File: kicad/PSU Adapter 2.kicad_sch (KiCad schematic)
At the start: 17 parts, among them J1 AC Connector, J2 ATX From PSU, J3 Power to Logic Board, J4 Fan, J5 Power to PSU, J6 Conn_01x05_Pin, K1 AC Passthrough Relay, U1 TLP521-1

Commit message: Add files via upload
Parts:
- removed J2: ATX From PSU, Connector_Molex:Molex_Mini-Fit_Jr_5566-20A_2x10_P4.20mm_Vertical, symbol Connector:ATX-20
- added J7: ATX-24, Connector_Molex:Molex_Mini-Fit_Jr_5566-24A_2x12_P4.20mm_Vertical, symbol Connector:ATX-24
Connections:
- net +12V: now also J7.10 (+12V), J7.11 (+12V)
- net +5V: now also J7.21 (+5V), J7.22 (+5V), J7.23 (+5V), J7.4 (+5V), J7.6 (+5V)
- net +5VSB: now also J7.9 (+5VSB)
- net -12V: now also J7.14 (-12V)
- net GND: now also J7.15 (GND), J7.17 (GND), J7.18 (GND), J7.19 (GND), J7.24 (GND), J7.3 (GND), J7.5 (GND), J7.7 (GND)
- net PS_ON: now also J7.16 (PS_ON#)
- net PWR_OK: now also J7.8 (PWR_OK)
- new net: J7.1 (+3.3V), J7.12 (+3.3V), J7.13 (+3.3V), J7.2 (+3.3V)
- no-connect marks 7 -> 6
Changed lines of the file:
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@@
+	)
+	(no_connect
+		(at 59.69 147.32)
+	)
+	(no_connect
+		(at 59.69 132.08)
+	)
+	(no_connect
+		(at 59.69 156.21)
+	)
+	(no_connect
+		(at 48.26 99.06)
 	)
 	(no_connect
@@
 	)
 	(no_connect
-		(at 59.69 147.32)
-	)
-	(no_connect
-		(at 59.69 132.08)
-	)
-	(no_connect
-		(at 59.69 156.21)
-	)
-	(no_connect
-		(at 48.26 99.06)
-	)
-	(no_connect
 		(at 59.69 139.7)
-	)
-	(no_connect
-		(at 162.56 106.68)
 	)
 	(wire
@@
 	)
 	(symbol
-		(lib_id "Connector:ATX-20")
+		(lib_id "Connector:ATX-24")
 		(at 149.86 99.06 0)
 		(unit 1)
@@
 		(dnp no)
 		(fields_autoplaced yes)
-		(property "Reference" "J2"
+		(property "Reference" "J7"
 			(at 149.86 81.28 0)
 			(effects
@@
 			)
 		)
-		(property "Value" "ATX From PSU"
+		(property "Value" "ATX-24"
 			(at 149.86 83.82 0)
 			(effects
@@
 			)
 		)
-		(property "Footprint" "Connector_Molex:Molex_Mini-Fit_Jr_5566-20A_2x10_P4.20mm_Vertical"
+		(property "Footprint" "Connector_Molex:Molex_Mini-Fit_Jr_5566-24A_2x12_P4.20mm_Vertical"
 			(at 149.86 101.6 0)
 			(effects
@@
 			)
 		)
-		(property "Datasheet" "https://web.aub.edu.lb/pub/docs/atx_201.pdf#page=20"
-			(at 177.8 113.03 0)
-			(effects
-				(font
-					(size 1.27 1.27)
-				)
-				(hide yes)
-			)
-		)
-		(property "Description" "ATX Power supply 20pins"
+		(property "Datasheet" "https://www.intel.com/content/dam/www/public/us/en/documents/guides/power-supply-design-guide-june.pdf#page=33"
+			(at 210.82 113.03 0)
+			(effects
+				(font
+					(size 1.27 1.27)
+				)
+				(hide yes)
+			)
+		)
+		(property "Description" "ATX Power supply 24pins"
 			(at 149.86 99.06 0)
 			(effects
@@
 			)
 		)
+		(pin "22"
+		)
+		(pin "4"
+		)
+		(pin "16"
+		)
+		(pin "6"
+		)
+		(pin "5"
+		)
+		(pin "24"
+		)
+		(pin "21"
+		)
+		(pin "3"
+		)
+		(pin "23"
+		)
+		(pin "17"
+		)
+		(pin "19"
+		)
+		(pin "9"
+		)
+		(pin "12"
+		)
+		(pin "18"
+		)
+		(pin "7"
+		)
+		(pin "1"
+		)
+		(pin "13"
+		)
+		(pin "14"
+		)
+		(pin "8"
+		)
+		(pin "10"
+		)
+		(pin "11"
+		)
 		(pin "2"
 		)
-		(pin "5"
+		(pin "15"
 		)
 		(pin "20"
-		)
-		(pin "8"
-		)
-		(pin "6"
-		)
-		(pin "7"
-		)
-		(pin "9"
-		)
-		(pin "4"
-		)
-		(pin "14"
-		)
-		(pin "15"
-		)
-		(pin "12"
-		)
-		(pin "18"
-		)
-		(pin "19"
-		)
-		(pin "17"
-		)
-		(pin "3"
-		)
-		(pin "16"
-		)
-		(pin "11"
-		)
-		(pin "10"
-		)
-		(pin "1"
-		)
-		(pin "13"
 		)
 		(instances
 			(project ""
 				(path "/aa6810f0-306b-47aa-aed9-06c517ff2e59"
-					(reference "J2")
+					(reference "J7")
 					(unit 1)
 				)

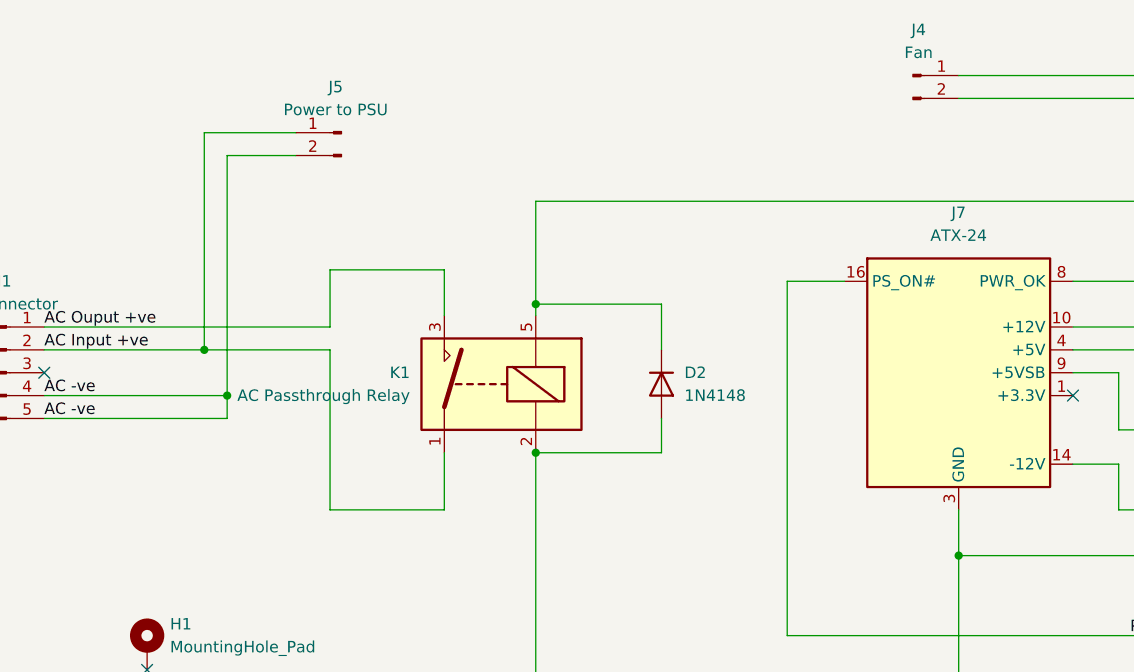
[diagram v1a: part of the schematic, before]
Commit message: Add files via upload
Updated to rev 0.3 including footprint for Chinese ATX connector which has 4.2mm pitch between rows (Molex spec is 5.5mm)
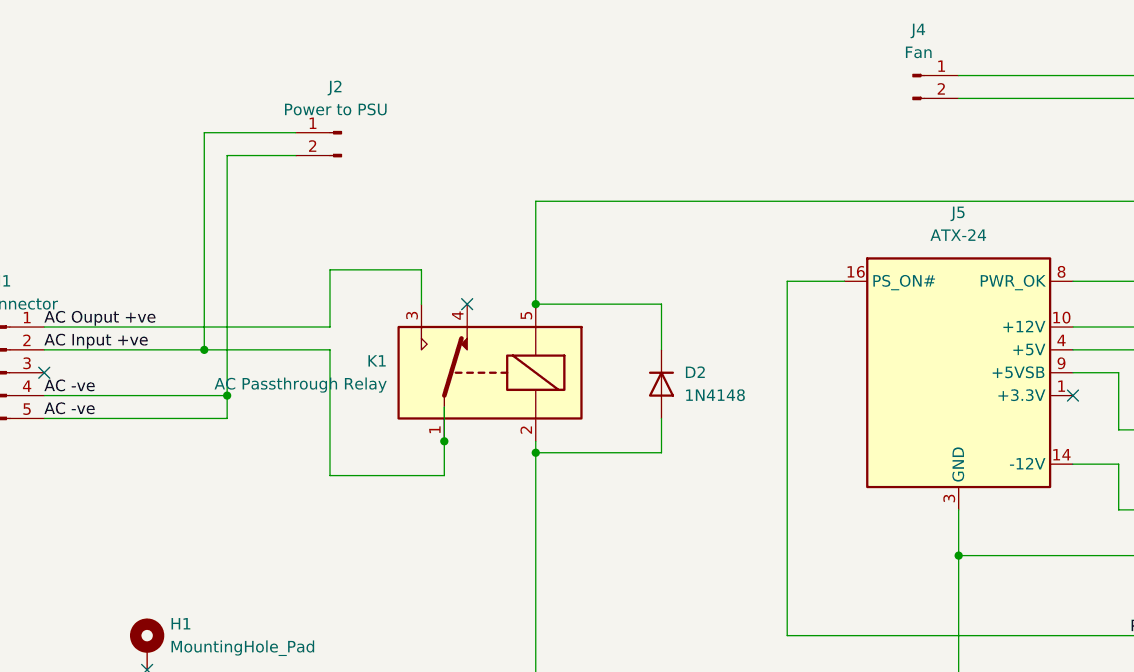
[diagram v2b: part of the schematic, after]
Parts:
- removed K1: AC Passthrough Relay, Relay_THT:Relay_SPST_SANYOU_SRD_Series_Form_A, symbol Relay:SANYOU_SRD_Form_A
- added K1: AC Passthrough Relay, Relay_THT:Relay_SPDT_SANYOU_SRD_Series_Form_C, symbol Relay:SANYOU_SRD_Form_C
- J4: footprint Connector_JST:JST_PH_B2B-PH-K_1x02_P2.00mm_Vertical -> Connector_JST:JST_XA_B02B-XASK-1-A_1x02_P2.50mm_Vertical
- renumbered J5 to J2, J7 to J5
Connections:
- net +12V: now also K1.5
- net AC Input +ve: now also K1.1
- net AC Ouput +ve: now also K1.3
- net GND: now also K1.2
- no-connect marks 6 -> 7
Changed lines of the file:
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@@
+	)
+	(junction
+		(at 177.8 123.19)
+		(diameter 0)
+		(color 0 0 0 0)
+	)
+	(junction
+		(at 233.68 101.6)
+		(diameter 0)
+		(color 0 0 0 0)
+	)
+	(junction
+		(at 149.86 134.62)
+		(diameter 0)
+		(color 0 0 0 0)
+	)
+	(junction
+		(at 177.8 73.66)
+		(diameter 0)
+		(color 0 0 0 0)
+	)
+	(junction
+		(at 92.71 106.68)
+		(diameter 0)
+		(color 0 0 0 0)
+	)
+	(junction
+		(at 173.99 80.01)
+		(diameter 0)
+		(color 0 0 0 0)
+	)
+	(junction
+		(at 200.66 130.81)
+		(diameter 0)
+		(color 0 0 0 0)
 	)
 	(junction
@@
 	)
 	(junction
-		(at 177.8 123.19)
-		(diameter 0)
-		(color 0 0 0 0)
-	)
-	(junction
-		(at 233.68 101.6)
-		(diameter 0)
-		(color 0 0 0 0)
-	)
-	(junction
-		(at 149.86 134.62)
-		(diameter 0)
-		(color 0 0 0 0)
-	)
-	(junction
-		(at 177.8 73.66)
-		(diameter 0)
-		(color 0 0 0 0)
-	)
-	(junction
-		(at 173.99 80.01)
-		(diameter 0)
-		(color 0 0 0 0)
-	)
-	(junction
-		(at 200.66 130.81)
-		(diameter 0)
-		(color 0 0 0 0)
-	)
-	(junction
 		(at 102.87 107.95)
 		(diameter 0)
@@
 	)
 	(no_connect
+		(at 95.25 91.44)
+	)
+	(no_connect
 		(at 162.56 101.6)
 	)
@@
 	(wire
 		(pts
-			(xy 80.01 96.52) (xy 80.01 114.3)
+			(xy 80.01 96.52) (xy 80.01 110.49)
 		)
 		(stroke
@@
 	(wire
 		(pts
-			(xy 92.71 87.63) (xy 92.71 92.71)
+			(xy 90.17 87.63) (xy 90.17 91.44)
 		)
 		(stroke
@@
 	(wire
 		(pts
-			(xy 102.87 91.44) (xy 102.87 92.71)
-		)
-		(stroke
-			(width 0)
-			(type default)
-		)
-	)
-	(wire
-		(pts
-			(xy 80.01 87.63) (xy 92.71 87.63)
+			(xy 102.87 106.68) (xy 102.87 107.95)
+		)
+		(stroke
+			(width 0)
+			(type default)
+		)
+	)
+	(wire
+		(pts
+			(xy 80.01 87.63) (xy 90.17 87.63)
 		)
 		(stroke
@@
 	(wire
 		(pts
-			(xy 92.71 114.3) (xy 80.01 114.3)
+			(xy 92.71 110.49) (xy 80.01 110.49)
 		)
 		(stroke
@@
 	(wire
 		(pts
-			(xy 92.71 107.95) (xy 92.71 114.3)
+			(xy 92.71 102.87) (xy 92.71 106.68)
 		)
 		(stroke
@@
 		(pts
 			(xy 116.84 104.14) (xy 116.84 107.95)
+		)
+		(stroke
+			(width 0)
+			(type default)
+		)
+	)
+	(wire
+		(pts
+			(xy 92.71 106.68) (xy 92.71 110.49)
 		)
 		(stroke
@@
 		(on_board yes)
 		(dnp no)
-		(property "Reference" "J5"
+		(property "Reference" "J2"
 			(at 80.645 67.31 0)
 			(effects
@@
 			(project ""
 				(path "/aa6810f0-306b-47aa-aed9-06c517ff2e59"
-					(reference "J5")
+					(reference "J2")
 					(unit 1)
 				)
@@
 				(path "/aa6810f0-306b-47aa-aed9-06c517ff2e59"
 					(reference "D2")
+					(unit 1)
+				)
+			)
+		)
+	)
+	(symbol
+		(lib_id "Relay:SANYOU_SRD_Form_C")
+		(at 97.79 99.06 0)
+		(mirror y)
+		(unit 1)
+		(exclude_from_sim no)
+		(in_bom yes)
+		(on_board yes)
+		(dnp no)
+		(property "Reference" "K1"
+			(at 86.36 97.7899 0)
+			(effects
+				(font
+					(size 1.27 1.27)
+				)
+				(justify left)
+			)
+		)
+		(property "Value" "AC Passthrough Relay"
+			(at 86.36 100.3299 0)
+			(effects
+				(font
+					(size 1.27 1.27)
+				)
+				(justify left)
+			)
+		)
+		(property "Footprint" "Relay_THT:Relay_SPDT_SANYOU_SRD_Series_Form_C"
+			(at 86.36 100.33 0)
+			(effects
+				(font
+					(size 1.27 1.27)
+				)
+				(justify left)
+				(hide yes)
+			)
+		)
+		(property "Datasheet" "http://www.sanyourelay.ca/public/products/pdf/SRD.pdf"
+			(at 97.79 99.06 0)
+			(effects
+				(font
+					(size 1.27 1.27)
+				)
+				(hide yes)
+			)
+		)
+		(property "Description" "Sanyo SRD relay, Single Pole Miniature Power Relay,"
+			(at 97.79 99.06 0)
+			(effects
+				(font
+					(size 1.27 1.27)
+				)
+				(hide yes)
+			)
+		)
+		(pin "3"
+		)
+		(pin "5"
+		)
+		(pin "2"
+		)
+		(pin "1"
+		)
+		(pin "4"
+		)
+		(instances
+			(project ""
+				(path "/aa6810f0-306b-47aa-aed9-06c517ff2e59"
+					(reference "K1")
 					(unit 1)
 				)
@@
 	)
 	(symbol
-		(lib_id "Relay:SANYOU_SRD_Form_A")
-		(at 97.79 100.33 0)
-		(mirror y)
-		(unit 1)
-		(exclude_from_sim no)
-		(in_bom yes)
-		(on_board yes)
-		(dnp no)
-		(property "Reference" "K1"
-			(at 88.9 99.0599 0)
-			(effects
-				(font
-					(size 1.27 1.27)
-				)
-				(justify left)
-			)
-		)
-		(property "Value" "AC Passthrough Relay"
-			(at 88.9 101.5999 0)
-			(effects
-				(font
-					(size 1.27 1.27)
-				)
-				(justify left)
-			)
-		)
-		(property "Footprint" "Relay_THT:Relay_SPST_SANYOU_SRD_Series_Form_A"
-			(at 88.9 101.6 0)
-			(effects
-				(font
-					(size 1.27 1.27)
-				)
-				(justify left)
-				(hide yes)
-			)
-		)
-		(property "Datasheet" "http://www.sanyourelay.ca/public/products/pdf/SRD.pdf"
-			(at 97.79 100.33 0)
-			(effects
-				(font
-					(size 1.27 1.27)
-				)
-				(hide yes)
-			)
-		)
-		(property "Description" "Sanyo SRD relay, Single Pole Miniature Power Relay, Closing Contact"
-			(at 97.79 100.33 0)
-			(effects
-				(font
-					(size 1.27 1.27)
-				)
-				(hide yes)
-			)
-		)
-		(pin "3"
-		)
-		(pin "2"
-		)
-		(pin "1"
-		)
-		(pin "5"
-		)
-		(instances
-			(project ""
-				(path "/aa6810f0-306b-47aa-aed9-06c517ff2e59"
-					(reference "K1")
-					(unit 1)
-				)
-			)
-		)
-	)
-	(symbol
 		(lib_id "Connector:ATX-24")
 		(at 149.86 99.06 0)
@@
 		(dnp no)
 		(fields_autoplaced yes)
-		(property "Reference" "J7"
+		(property "Reference" "J5"
 			(at 149.86 81.28 0)
 			(effects
@@
 			(project ""
 				(path "/aa6810f0-306b-47aa-aed9-06c517ff2e59"
-					(reference "J7")
+					(reference "J5")
 					(unit 1)
 				)
@@
 			)
 		)
-		(property "Footprint" "Connector_JST:JST_PH_B2B-PH-K_1x02_P2.00mm_Vertical"
+		(property "Footprint" "Connector_JST:JST_XA_B02B-XASK-1-A_1x02_P2.50mm_Vertical"
 			(at 144.78 66.04 0)
 			(effects

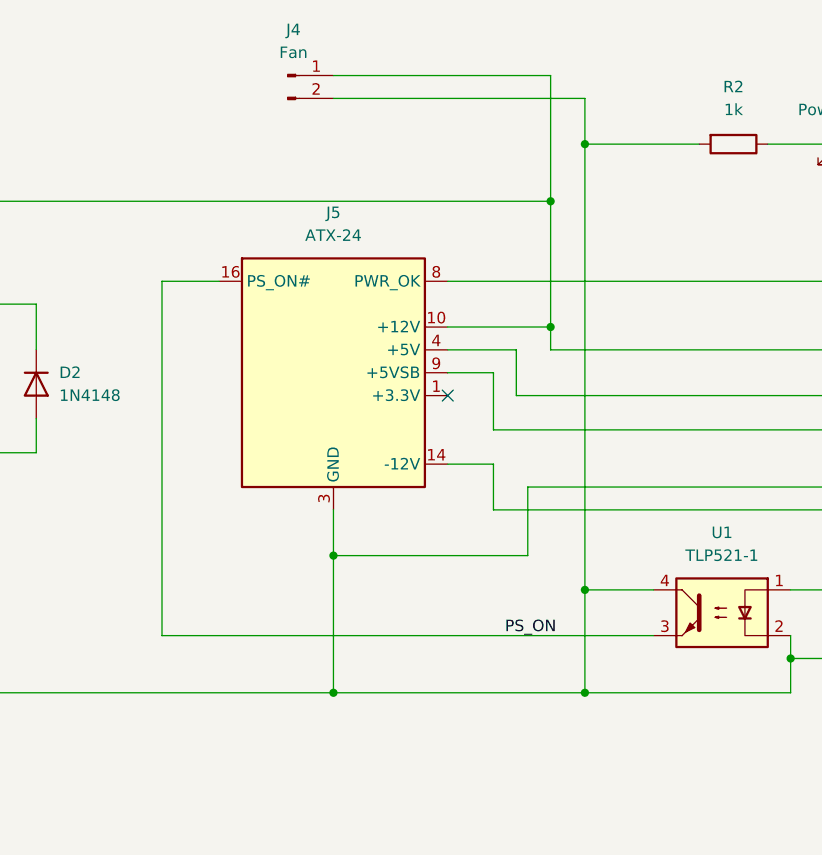
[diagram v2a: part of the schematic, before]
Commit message: Add files via upload
Fix soft start
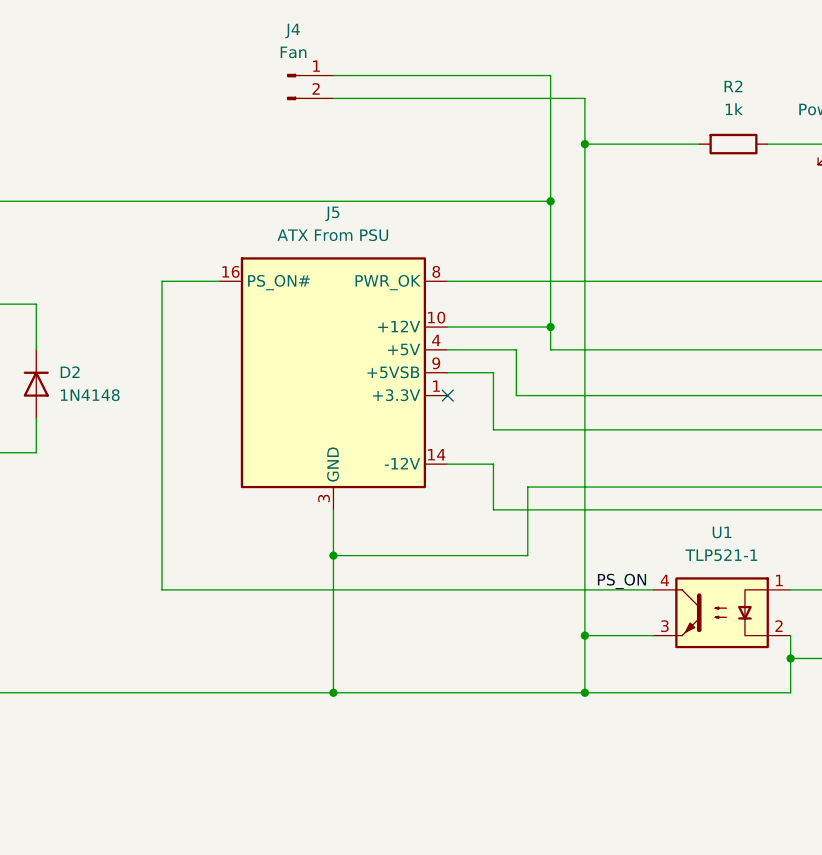
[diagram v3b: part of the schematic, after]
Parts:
- J4: footprint Connector_JST:JST_XA_B02B-XASK-1-A_1x02_P2.50mm_Vertical -> Connector_JST:JST_XA_B02B-XASK-1_1x02_P2.50mm_Vertical
- J5: value ATX-24 -> ATX From PSU; footprint Connector_Molex:Molex_Mini-Fit_Jr_5566-24A_2x12_P4.20mm_Vertical -> Library:Molex_Mini-Fit_Jr_5566-24A_2x12_P4.20mm_Vertical_Chinese
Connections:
- net GND: now also U1.3; no longer U1.4
- net PS_ON: now also U1.4; no longer U1.3
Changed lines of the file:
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@@
 	)
 	(junction
-		(at 177.8 123.19)
+		(at 177.8 128.27)
 		(diameter 0)
 		(color 0 0 0 0)
@@
 	(wire
 		(pts
-			(xy 177.8 123.19) (xy 185.42 123.19)
-		)
-		(stroke
-			(width 0)
-			(type default)
-		)
-	)
-	(wire
-		(pts
 			(xy 177.8 134.62) (xy 200.66 134.62)
 		)
@@
 	(wire
 		(pts
-			(xy 177.8 73.66) (xy 177.8 123.19)
-		)
-		(stroke
-			(width 0)
-			(type default)
-		)
-	)
-	(wire
-		(pts
 			(xy 200.66 128.27) (xy 200.66 130.81)
 		)
@@
 	(wire
 		(pts
+			(xy 177.8 128.27) (xy 185.42 128.27)
+		)
+		(stroke
+			(width 0)
+			(type default)
+		)
+	)
+	(wire
+		(pts
 			(xy 162.56 109.22) (xy 167.64 109.22)
 		)
@@
 	(wire
 		(pts
-			(xy 177.8 123.19) (xy 177.8 134.62)
+			(xy 177.8 73.66) (xy 177.8 128.27)
 		)
 		(stroke
@@
 	(wire
 		(pts
+			(xy 177.8 128.27) (xy 177.8 134.62)
+		)
+		(stroke
+			(width 0)
+			(type default)
+		)
+	)
+	(wire
+		(pts
 			(xy 246.38 104.14) (xy 233.68 104.14)
 		)
@@
 	(wire
 		(pts
-			(xy 130.81 88.9) (xy 130.81 128.27)
-		)
-		(stroke
-			(width 0)
-			(type default)
-		)
-	)
-	(wire
-		(pts
 			(xy 190.5 73.66) (xy 177.8 73.66)
 		)
@@
 	(wire
 		(pts
+			(xy 130.81 88.9) (xy 130.81 123.19)
+		)
+		(stroke
+			(width 0)
+			(type default)
+		)
+	)
+	(wire
+		(pts
 			(xy 130.81 88.9) (xy 137.16 88.9)
 		)
@@
 	(wire
 		(pts
+			(xy 130.81 123.19) (xy 185.42 123.19)
+		)
+		(stroke
+			(width 0)
+			(type default)
+		)
+	)
+	(wire
+		(pts
 			(xy 92.71 106.68) (xy 92.71 110.49)
 		)
@@
 		(pts
 			(xy 149.86 66.04) (xy 173.99 66.04)
-		)
-		(stroke
-			(width 0)
-			(type default)
-		)
-	)
-	(wire
-		(pts
-			(xy 130.81 128.27) (xy 185.42 128.27)
 		)
 		(stroke
@@
 		)
 	)
-	(label "PS_ON"
-		(at 168.91 128.27 0)
+	(label "GND"
+		(at 223.52 111.76 0)
 		(fields_autoplaced yes)
 		(effects
@@
 		)
 	)
-	(label "GND"
-		(at 223.52 111.76 0)
+	(label "AC Input +ve"
+		(at 48.26 96.52 0)
 		(fields_autoplaced yes)
 		(effects
@@
 		)
 	)
-	(label "AC Input +ve"
-		(at 48.26 96.52 0)
+	(label "PS_ON"
+		(at 179.07 123.19 0)
 		(fields_autoplaced yes)
 		(effects
@@
 			)
 		)
-		(property "Value" "ATX-24"
+		(property "Value" "ATX From PSU"
 			(at 149.86 83.82 0)
 			(effects
@@
 			)
 		)
-		(property "Footprint" "Connector_Molex:Molex_Mini-Fit_Jr_5566-24A_2x12_P4.20mm_Vertical"
+		(property "Footprint" "Library:Molex_Mini-Fit_Jr_5566-24A_2x12_P4.20mm_Vertical_Chinese"
 			(at 149.86 101.6 0)
 			(effects
@@
 			)
 		)
-		(property "Footprint" "Connector_JST:JST_XA_B02B-XASK-1-A_1x02_P2.50mm_Vertical"
+		(property "Footprint" "Connector_JST:JST_XA_B02B-XASK-1_1x02_P2.50mm_Vertical"
 			(at 144.78 66.04 0)
 			(effects
